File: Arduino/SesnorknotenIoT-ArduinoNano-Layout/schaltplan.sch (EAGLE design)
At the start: 10 parts

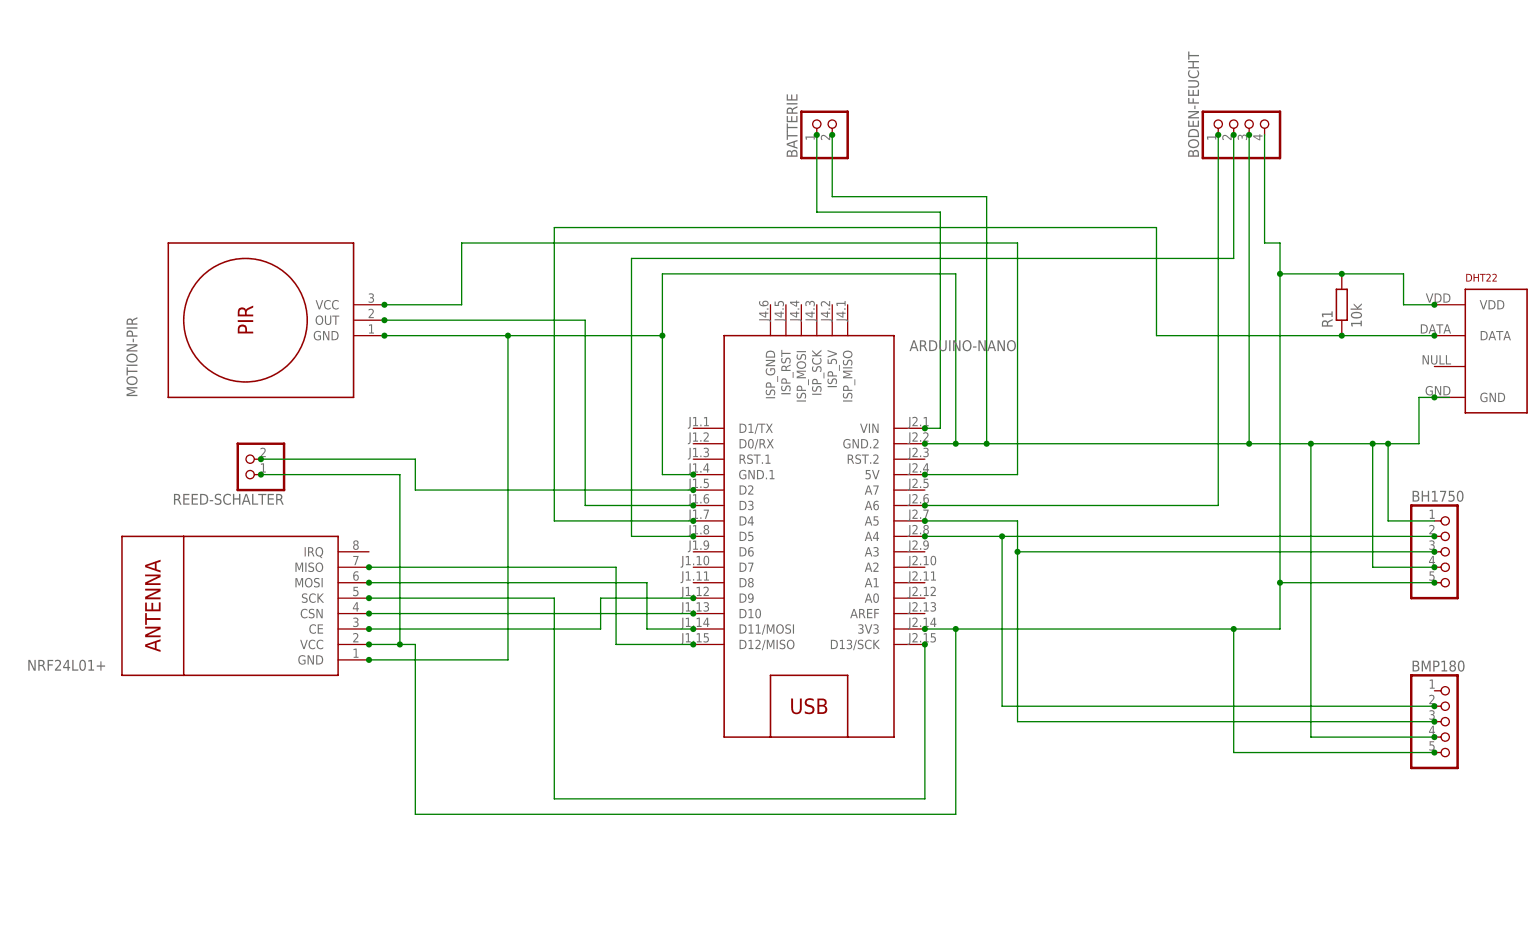
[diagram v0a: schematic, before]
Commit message: Eagle +Reed Schalter +1-Wire +Schalter stromversorgung
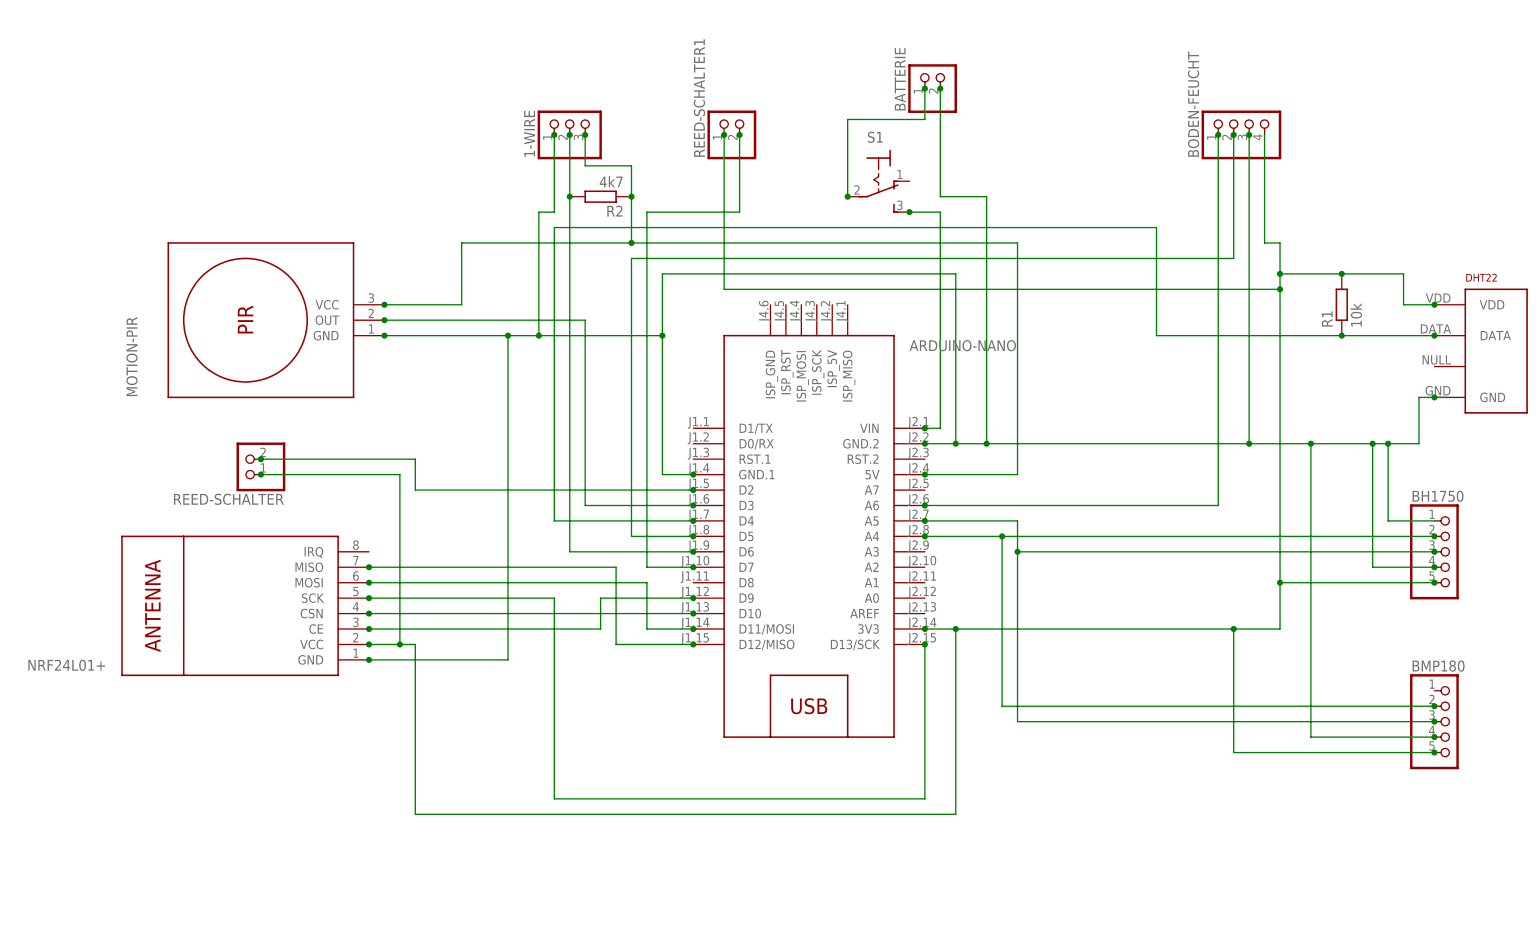
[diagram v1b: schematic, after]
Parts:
- added 1-WIRE: (no value), pinhead:PINHD-1X3
- added R2: 4k7, resistor:R-EU_0207/10
- added REED-SCHALTER1: (no value), pinhead:PINHD-1X2
- added S1: (no value), switch:320-916
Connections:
- new net N$5: BATTERIE.1, S1.P
- new net N$6: 1-WIRE.2, ARDUINO-NANO.D6, R2.2
- new net N$7: ARDUINO-NANO.D7, REED-SCHALTER1.2
- net 3.3V: now also REED-SCHALTER1.1
- net 5V: now also 1-WIRE.3, R2.1
- net GND: now also 1-WIRE.1
- net N$13: now also S1.S; no longer BATTERIE.1
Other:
- moved on the sheet: BATTERIE
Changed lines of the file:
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@@
 <part name="REED-SCHALTER" library="pinhead" deviceset="PINHD-1X2" device=""/>
 <part name="BODEN-FEUCHT" library="pinhead" deviceset="PINHD-1X4" device=""/>
+<part name="1-WIRE" library="pinhead" deviceset="PINHD-1X3" device=""/>
+<part name="R2" library="resistor" deviceset="R-EU_" device="0207/10" value="4k7"/>
+<part name="S1" library="switch" deviceset="320-916" device=""/>
+<part name="REED-SCHALTER1" library="pinhead" deviceset="PINHD-1X2" device=""/>
 </parts>
 <sheets>
@@
 <instance part="DHT22" gate="G$1" x="172.72" y="78.74"/>
 <instance part="R1" gate="G$1" x="147.32" y="86.36" rot="R90"/>
-<instance part="BATTERIE" gate="G$1" x="63.5" y="116.84" rot="R90"/>
+<instance part="BATTERIE" gate="G$1" x="81.28" y="124.46" rot="R90"/>
 <instance part="BMP180" gate="A" x="165.1" y="17.78"/>
 <instance part="BH1750" gate="A" x="165.1" y="45.72"/>
 <instance part="REED-SCHALTER" gate="G$1" x="-33.02" y="60.96" rot="R180"/>
 <instance part="BODEN-FEUCHT" gate="A" x="132.08" y="116.84" rot="R90"/>
+<instance part="1-WIRE" gate="A" x="20.32" y="116.84" rot="R90"/>
+<instance part="R2" gate="G$1" x="25.4" y="104.14" rot="R180"/>
+<instance part="S1" gate="1" x="71.12" y="106.68" rot="R270"/>
+<instance part="REED-SCHALTER1" gate="G$1" x="48.26" y="116.84" rot="R90"/>
 </instances>
 <busses>
@@
 <wire x1="129.54" y1="33.02" x2="137.16" y2="33.02" width="0.1524" layer="91"/>
 <wire x1="137.16" y1="33.02" x2="137.16" y2="40.64" width="0.1524" layer="91"/>
-<wire x1="137.16" y1="40.64" x2="137.16" y2="91.44" width="0.1524" layer="91"/>
+<wire x1="137.16" y1="40.64" x2="137.16" y2="88.9" width="0.1524" layer="91"/>
+<wire x1="137.16" y1="88.9" x2="137.16" y2="91.44" width="0.1524" layer="91"/>
 <wire x1="137.16" y1="91.44" x2="147.32" y2="91.44" width="0.1524" layer="91"/>
 <wire x1="147.32" y1="91.44" x2="157.48" y2="91.44" width="0.1524" layer="91"/>
@@
 <wire x1="137.16" y1="96.52" x2="137.16" y2="91.44" width="0.1524" layer="91"/>
 <junction x="137.16" y="91.44"/>
+<pinref part="REED-SCHALTER1" gate="G$1" pin="1"/>
+<wire x1="137.16" y1="88.9" x2="45.72" y2="88.9" width="0.1524" layer="91"/>
+<wire x1="45.72" y1="88.9" x2="45.72" y2="114.3" width="0.1524" layer="91"/>
+<junction x="137.16" y="88.9"/>
+<junction x="45.72" y="114.3"/>
 </segment>
 </net>
@@
 <wire x1="162.56" y1="71.12" x2="165.1" y2="71.12" width="0.1524" layer="91"/>
 <wire x1="-10.16" y1="81.28" x2="10.16" y2="81.28" width="0.1524" layer="91"/>
-<wire x1="10.16" y1="81.28" x2="35.56" y2="81.28" width="0.1524" layer="91"/>
+<wire x1="10.16" y1="81.28" x2="15.24" y2="81.28" width="0.1524" layer="91"/>
+<wire x1="15.24" y1="81.28" x2="35.56" y2="81.28" width="0.1524" layer="91"/>
 <wire x1="35.56" y1="81.28" x2="35.56" y2="91.44" width="0.1524" layer="91"/>
 <wire x1="35.56" y1="91.44" x2="83.82" y2="91.44" width="0.1524" layer="91"/>
@@
 <junction x="78.74" y="63.5"/>
 <pinref part="BATTERIE" gate="G$1" pin="2"/>
-<wire x1="63.5" y1="114.3" x2="63.5" y2="104.14" width="0.1524" layer="91"/>
-<wire x1="63.5" y1="104.14" x2="88.9" y2="104.14" width="0.1524" layer="91"/>
+<wire x1="81.28" y1="121.92" x2="81.28" y2="104.14" width="0.1524" layer="91"/>
+<wire x1="81.28" y1="104.14" x2="88.9" y2="104.14" width="0.1524" layer="91"/>
 <wire x1="88.9" y1="104.14" x2="88.9" y2="63.5" width="0.1524" layer="91"/>
 <junction x="88.9" y="63.5"/>
@@
 <pinref part="DHT22" gate="G$1" pin="GND"/>
 <junction x="162.56" y="71.12"/>
-<junction x="63.5" y="114.3"/>
+<junction x="81.28" y="121.92"/>
 <wire x1="35.56" y1="81.28" x2="35.56" y2="58.42" width="0.1524" layer="91"/>
 <pinref part="ARDUINO-NANO" gate="G$1" pin="GND.1"/>
@@
 <junction x="132.08" y="114.3"/>
 <junction x="132.08" y="63.5"/>
+<pinref part="1-WIRE" gate="A" pin="1"/>
+<wire x1="17.78" y1="114.3" x2="17.78" y2="101.6" width="0.1524" layer="91"/>
+<wire x1="17.78" y1="101.6" x2="15.24" y2="101.6" width="0.1524" layer="91"/>
+<wire x1="15.24" y1="101.6" x2="15.24" y2="81.28" width="0.1524" layer="91"/>
+<junction x="15.24" y="81.28"/>
+<junction x="17.78" y="114.3"/>
 </segment>
 </net>
@@
 <wire x1="78.74" y1="58.42" x2="93.98" y2="58.42" width="0.1524" layer="91"/>
 <wire x1="93.98" y1="58.42" x2="93.98" y2="96.52" width="0.1524" layer="91"/>
-<wire x1="93.98" y1="96.52" x2="2.54" y2="96.52" width="0.1524" layer="91"/>
+<wire x1="93.98" y1="96.52" x2="30.48" y2="96.52" width="0.1524" layer="91"/>
+<wire x1="30.48" y1="96.52" x2="2.54" y2="96.52" width="0.1524" layer="91"/>
 <wire x1="2.54" y1="96.52" x2="2.54" y2="86.36" width="0.1524" layer="91"/>
 <pinref part="MOTION-PIR" gate="G$1" pin="VCC"/>
@@
 <junction x="-10.16" y="86.36"/>
 <junction x="78.74" y="58.42"/>
+<pinref part="1-WIRE" gate="A" pin="3"/>
+<wire x1="22.86" y1="114.3" x2="22.86" y2="109.22" width="0.1524" layer="91"/>
+<wire x1="22.86" y1="109.22" x2="30.48" y2="109.22" width="0.1524" layer="91"/>
+<wire x1="30.48" y1="109.22" x2="30.48" y2="104.14" width="0.1524" layer="91"/>
+<pinref part="R2" gate="G$1" pin="1"/>
+<junction x="30.48" y="104.14"/>
+<wire x1="30.48" y1="104.14" x2="30.48" y2="96.52" width="0.1524" layer="91"/>
+<junction x="22.86" y="114.3"/>
+<junction x="30.48" y="96.52"/>
 </segment>
 </net>
@@
 <net name="N$13" class="0">
 <segment>
-<pinref part="BATTERIE" gate="G$1" pin="1"/>
-<wire x1="60.96" y1="114.3" x2="60.96" y2="101.6" width="0.1524" layer="91"/>
-<wire x1="60.96" y1="101.6" x2="81.28" y2="101.6" width="0.1524" layer="91"/>
 <wire x1="81.28" y1="101.6" x2="81.28" y2="66.04" width="0.1524" layer="91"/>
 <pinref part="ARDUINO-NANO" gate="G$1" pin="VIN"/>
 <wire x1="81.28" y1="66.04" x2="78.74" y2="66.04" width="0.1524" layer="91"/>
 <junction x="78.74" y="66.04"/>
-<junction x="60.96" y="114.3"/>
+<wire x1="81.28" y1="101.6" x2="76.2" y2="101.6" width="0.1524" layer="91"/>
+<pinref part="S1" gate="1" pin="S"/>
+<junction x="76.2" y="101.6"/>
 </segment>
 </net>
@@
 </segment>
 </net>
+<net name="N$6" class="0">
+<segment>
+<pinref part="ARDUINO-NANO" gate="G$1" pin="D6"/>
+<pinref part="1-WIRE" gate="A" pin="2"/>
+<wire x1="40.64" y1="45.72" x2="20.32" y2="45.72" width="0.1524" layer="91"/>
+<wire x1="20.32" y1="45.72" x2="20.32" y2="104.14" width="0.1524" layer="91"/>
+<junction x="20.32" y="114.3"/>
+<junction x="40.64" y="45.72"/>
+<pinref part="R2" gate="G$1" pin="2"/>
+<wire x1="20.32" y1="104.14" x2="20.32" y2="114.3" width="0.1524" layer="91"/>
+<junction x="20.32" y="104.14"/>
+</segment>
+</net>
+<net name="N$5" class="0">
+<segment>
+<pinref part="BATTERIE" gate="G$1" pin="1"/>
+<wire x1="78.74" y1="121.92" x2="78.74" y2="116.84" width="0.1524" layer="91"/>
+<wire x1="78.74" y1="116.84" x2="66.04" y2="116.84" width="0.1524" layer="91"/>
+<wire x1="66.04" y1="116.84" x2="66.04" y2="104.14" width="0.1524" layer="91"/>
+<junction x="78.74" y="121.92"/>
+<pinref part="S1" gate="1" pin="P"/>
+<junction x="66.04" y="104.14"/>
+</segment>
+</net>
+<net name="N$7" class="0">
+<segment>
+<pinref part="ARDUINO-NANO" gate="G$1" pin="D7"/>
+<wire x1="40.64" y1="43.18" x2="33.02" y2="43.18" width="0.1524" layer="91"/>
+<wire x1="33.02" y1="43.18" x2="33.02" y2="101.6" width="0.1524" layer="91"/>
+<pinref part="REED-SCHALTER1" gate="G$1" pin="2"/>
+<wire x1="33.02" y1="101.6" x2="48.26" y2="101.6" width="0.1524" layer="91"/>
+<wire x1="48.26" y1="101.6" x2="48.26" y2="114.3" width="0.1524" layer="91"/>
+<junction x="48.26" y="114.3"/>
+<junction x="40.64" y="43.18"/>
+</segment>
+</net>

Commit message: Anpassungen Sensoren +Bewegungsmelder +nur Auswertung wenn die Sensoren angeschlossen sind
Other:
- note added: "Studienarbeit 2016/2017"
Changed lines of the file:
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@@
 <layer number="54" name="bGND_GNDA" color="7" fill="1" visible="no" active="no"/>
 <layer number="56" name="wert" color="7" fill="1" visible="no" active="no"/>
+<layer number="57" name="tCAD" color="7" fill="1" visible="no" active="no"/>
+<layer number="59" name="tCarbon" color="7" fill="1" visible="no" active="no"/>
+<layer number="60" name="bCarbon" color="7" fill="1" visible="no" active="no"/>
 <layer number="90" name="Modules" color="5" fill="1" visible="yes" active="yes"/>
 <layer number="91" name="Nets" color="2" fill="1" visible="yes" active="yes"/>
@@
 <layer number="108" name="tplace-old" color="7" fill="1" visible="yes" active="yes"/>
 <layer number="109" name="ref-old" color="7" fill="1" visible="yes" active="yes"/>
+<layer number="110" name="fp0" color="7" fill="1" visible="yes" active="yes"/>
+<layer number="111" name="LPC17xx" color="7" fill="1" visible="yes" active="yes"/>
+<layer number="112" name="tSilk" color="7" fill="1" visible="yes" active="yes"/>
+<layer number="113" name="IDFDebug" color="4" fill="1" visible="yes" active="yes"/>
 <layer number="116" name="Patch_BOT" color="7" fill="1" visible="yes" active="yes"/>
 <layer number="121" name="_tsilk" color="7" fill="1" visible="yes" active="yes"/>
 <layer number="122" name="_bsilk" color="7" fill="1" visible="yes" active="yes"/>
+<layer number="123" name="tTestmark" color="7" fill="1" visible="yes" active="yes"/>
+<layer number="124" name="bTestmark" color="7" fill="1" visible="yes" active="yes"/>
 <layer number="125" name="_tNames" color="7" fill="1" visible="yes" active="yes"/>
+<layer number="126" name="_bNames" color="7" fill="1" visible="yes" active="yes"/>
+<layer number="127" name="_tValues" color="7" fill="1" visible="yes" active="yes"/>
+<layer number="128" name="_bValues" color="7" fill="1" visible="yes" active="yes"/>
+<layer number="129" name="Mask" color="7" fill="1" visible="yes" active="yes"/>
+<layer number="131" name="tAdjust" color="7" fill="1" visible="yes" active="yes"/>
+<layer number="132" name="bAdjust" color="7" fill="1" visible="yes" active="yes"/>
 <layer number="144" name="Drill_legend" color="7" fill="1" visible="yes" active="yes"/>
+<layer number="150" name="Notes" color="7" fill="1" visible="yes" active="yes"/>
 <layer number="151" name="HeatSink" color="7" fill="1" visible="yes" active="yes"/>
+<layer number="152" name="_bDocu" color="7" fill="1" visible="yes" active="yes"/>
+<layer number="153" name="FabDoc1" color="7" fill="1" visible="yes" active="yes"/>
+<layer number="154" name="FabDoc2" color="7" fill="1" visible="yes" active="yes"/>
+<layer number="155" name="FabDoc3" color="7" fill="1" visible="yes" active="yes"/>
 <layer number="199" name="Contour" color="7" fill="1" visible="yes" active="yes"/>
 <layer number="200" name="200bmp" color="7" fill="1" visible="yes" active="yes"/>
@@
 <layer number="223" name="223bmp" color="7" fill="1" visible="yes" active="yes"/>
 <layer number="224" name="224bmp" color="7" fill="1" visible="yes" active="yes"/>
+<layer number="225" name="225bmp" color="7" fill="1" visible="yes" active="yes"/>
+<layer number="226" name="226bmp" color="7" fill="1" visible="yes" active="yes"/>
+<layer number="227" name="227bmp" color="7" fill="1" visible="yes" active="yes"/>
+<layer number="228" name="228bmp" color="7" fill="1" visible="yes" active="yes"/>
+<layer number="229" name="229bmp" color="7" fill="1" visible="yes" active="yes"/>
+<layer number="230" name="230bmp" color="7" fill="1" visible="yes" active="yes"/>
+<layer number="231" name="231bmp" color="7" fill="1" visible="yes" active="yes"/>
+<layer number="248" name="Housing" color="7" fill="1" visible="yes" active="yes"/>
+<layer number="249" name="Edge" color="7" fill="1" visible="yes" active="yes"/>
 <layer number="250" name="Descript" color="7" fill="1" visible="yes" active="yes"/>
 <layer number="251" name="SMDround" color="7" fill="1" visible="yes" active="yes"/>
 <layer number="254" name="cooling" color="7" fill="1" visible="yes" active="yes"/>
+<layer number="255" name="routoute" color="7" fill="1" visible="yes" active="yes"/>
 </layers>
 <schematic xreflabel="%F%N/%S.%C%R" xrefpart="/%S.%C%R">
+<description>Schaltplan SensorknotenIoT Arduino Nano</description>
 <attributes>
+<attribute name="CNAME" value="SensorknotenIoT Arduino Nano"/>
+<attribute name="CREVISION" value="2.3"/>
+<attribute name="DESIGNER" value="Jan G. &amp; David P."/>
 </attributes>
 <variantdefs>
@@
 <part name="S1" library="switch" deviceset="320-916" device=""/>
 <part name="REED-SCHALTER1" library="pinhead" deviceset="PINHD-1X2" device=""/>
+<part name="FRAME1" library="SparkFun-Aesthetics" deviceset="FRAME-A4L" device=""/>
 </parts>
 <sheets>
 <sheet>
 <plain>
+<text x="102.87" y="-13.97" size="2.54" layer="94" font="vector">Studienarbeit 2016/2017</text>
 </plain>
 <instances>
@@
 <instance part="S1" gate="1" x="71.12" y="106.68" rot="R270"/>
 <instance part="REED-SCHALTER1" gate="G$1" x="48.26" y="116.84" rot="R90"/>
+<instance part="FRAME1" gate="G$1" x="-78.74" y="-30.48" smashed="yes">
+<attribute name="LAST_DATE_TIME" x="102.87" y="-24.13" size="2.286" layer="94" font="vector"/>
+<attribute name="SHEET" x="116.84" y="-29.21" size="2.54" layer="94" font="vector"/>
+<attribute name="CNAME" x="102.87" y="-19.05" size="2.54" layer="94" font="vector"/>
+<attribute name="DESIGNER" x="147.52" y="-24.13" size="2.54" layer="94" font="vector"/>
+<attribute name="CREVISION" x="156.18" y="-29.31" size="2.54" layer="94" font="vector"/>
+</instance>
 </instances>
 <busses>
